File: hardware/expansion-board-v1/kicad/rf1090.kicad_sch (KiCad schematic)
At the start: 49 parts, among them J6 U.FL_1090_EXT(经尾线转SMA), J7 IFA_1090, Q3 AO3401A, U11 QPL9547TR7, U12 BGA2817, U13 AD8319ACPZ-R7(主), U14 AD8313ARMZ(备,二选一), U15 TLV3501(TOKMAS), U16 XA17-G4K(或AS179-92LF)

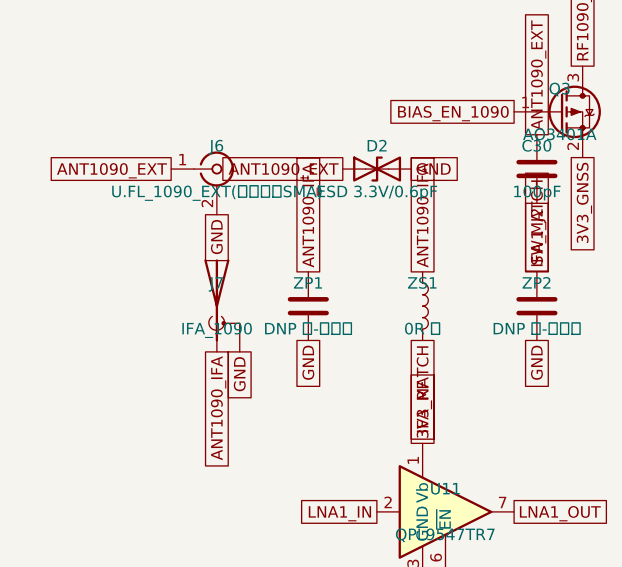
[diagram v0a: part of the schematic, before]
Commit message: feat(hw): 布局冻结为设计数据 + 丝印对齐机检 + 板名改 Avionics Board
## 布局所有权转移
区域装箱器的任务已完成——它把 152 个元件从零摆到可用起点。
用户人工精修了 81 个元件（把 CC1312R 去耦聚拢、978 直流侧贴近 J1 等，
装箱器摆不出来的判断）。精修后坐标即设计本身，不该再被算法覆盖。

  tools/export_placement.py  读 PCB → 行吸附 → 产出 PLACEMENT.py（只读源板）
  tools/PLACEMENT.py         156 元件 + 156 位号坐标，**设计数据不是生成物**
  gen_pcb.py / gen_silk.py   改为按 PLACEMENT.py 摆位；装箱与试位降级为新件兜底

往返验证：139/156 逐值一致，17 处差异恰为吸附项，无意外漂移。

## 对齐吸附（人工对不准，必须靠算法）
判据：同簇 = y 差 ≤0.35mm 且 x 间距 ≤12mm；目标取众数而非中位数
（多数已对齐、少数漂了，中位数会把对好的拽歪）。
实例：用户手拉 L14 行到 66.500，而 Q5 行是 66.553——肉眼差了 0.053mm。

## 新增三道丝印机检（这些问题此前靠人眼发现，漏过多次）
- 位号不得压在自己元件本体上（大件豁免）
- 同行 + 同高 + 同侧的位号绝对 y 必须一致
- 行对齐 pass 的每个候选位置都要过 压本体/压焊盘/压文字 三项

## 修掉的缺陷
- 冻结时把**失败状态**也固化：F.Fab 与"位号压本体"是算法状态不是设计意图，
  冻结导致永不重试（C62/C16/C17 因此永远没有位号）。改为只冻结成功项。
- 曾把行对齐写进 export_placement.py 盲改（那里没有障碍模型），
  把位号推到焊盘和丝印轮廓上（重叠 5→17、压铜 5→28）。对齐移入 gen_silk.py。
- C61/C66 两行下移 0.5mm：上一行本体底 94.33 与本行本体顶 95.72 净空仅 1.39mm，
  而位号需 0.5+1.1=1.6mm。

## 其它
- 板名 ADS-B Expansion → Avionics Board（功能已含 GNSS/IMU/BARO，不止 ADS-B）
- 背面丝印加 https://air.club
- J7 → ANT1（J 前缀属连接器，天线应用 ANT）
- tools/render.sh 出顶/底 3D + 分层 SVG + 装配图 PDF

状态：铜层 DRC 0 违例；丝印 2 出界 + 5 重叠；位号 156/156 全上板；布线未开始。
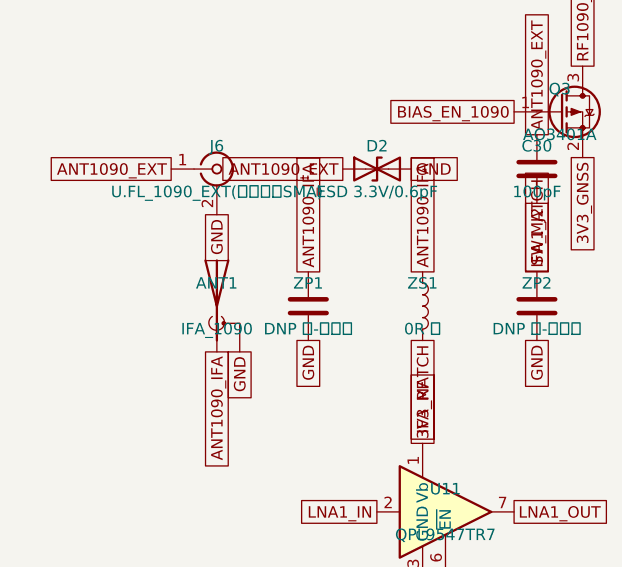
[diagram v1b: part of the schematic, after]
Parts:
- removed J7: IFA_1090, expansion-board-v1:ANT_IFA_1090MHz, symbol Device:Antenna_Shield
- added ANT1: IFA_1090, expansion-board-v1:ANT_IFA_1090MHz, symbol Device:Antenna_Shield
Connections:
- net ANT1090_IFA: now also ANT1.1 (A)
- net GND: now also ANT1.2 (Shield)
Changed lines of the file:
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@@
 		(on_board yes)
 		(dnp no)
-		(property "Reference" "J7"
+		(property "Reference" "ANT1"
 			(at 38.1 63.5 0)
 			(effects (font (size 1.27 1.27)))
@@
 			(project "expansion-board-v1"
 				(path "/10000000-0000-4000-8000-000000000001/20000000-0000-4000-8000-000000000003"
-					(reference "J7")
+					(reference "ANT1")
 					(unit 1)
 				)
